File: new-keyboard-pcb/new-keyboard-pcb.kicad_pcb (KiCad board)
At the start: 2 copper layers, 392.5 x 125.2 mm, 226 parts, among them J1 Conn_ARM_JTAG_SWD_10, J2 Conn_01x05_Socket, J3 Conn_01x05_Pin, J4 Conn_01x05_Socket, J5 Conn_01x05_Pin, SW1 ESC, SW10 F9, SW100 SW_Push_Dual, SW11 F10, SW12 F11, SW13 F12, SW14 PWR, SW15 NUMLCK, SW16 DIV, SW17 MULT, SW18 SUB, SW19 /, SW2 F1, SW20 1, SW21 2, SW22 3, SW23 4, SW24 5, SW25 6, SW26 7, SW27 8, SW28 9, SW29 0, SW3 F2, SW30 -, SW31 =, SW32 DEL, SW33 #7, SW34 #8, SW35 #9, SW36 TAB, SW37 Q, SW38 W, SW39 E, SW4 F3, SW40 R, SW41 T, SW42 Y, SW43 U, SW44 I, SW45 O, SW46 P, SW47 ^, SW48 Ç, SW49 ENTER, SW5 F4, SW50 #4, SW51 #5, SW52 #6, SW53 ADD, SW54 CAPSLCK, SW55 A, SW56 S, SW57 D, SW58 F, SW59 G, SW6 F5, SW60 H, SW61 J, SW62 K, SW63 L, SW64 ;, SW65 È, SW66 À, SW67 ENTER, SW68 #1, SW69 #2, SW7 F6, SW70 #3, SW71 #ENTER, SW72 LSHFT, SW73 Ù, SW74 Z, SW75 X, SW76 C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

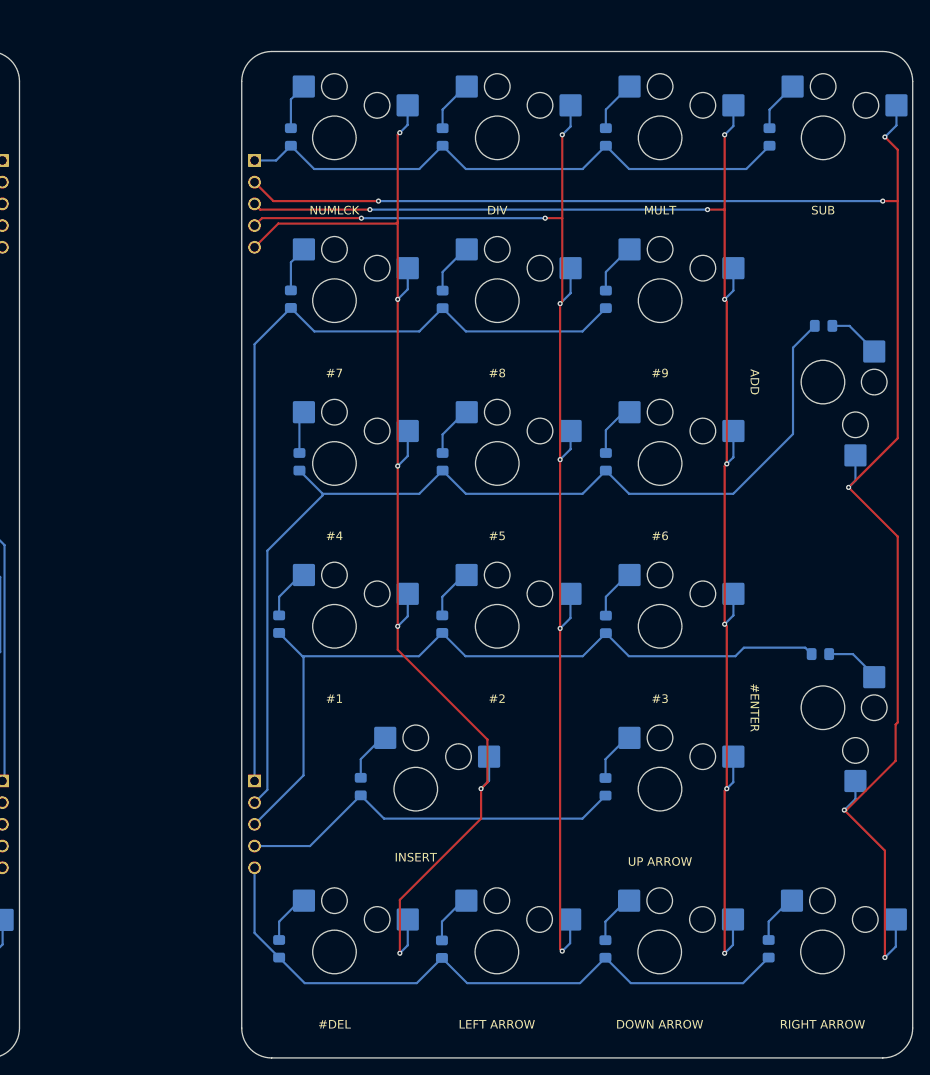
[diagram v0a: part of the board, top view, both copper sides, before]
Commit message: Correcting pogo connector connexions
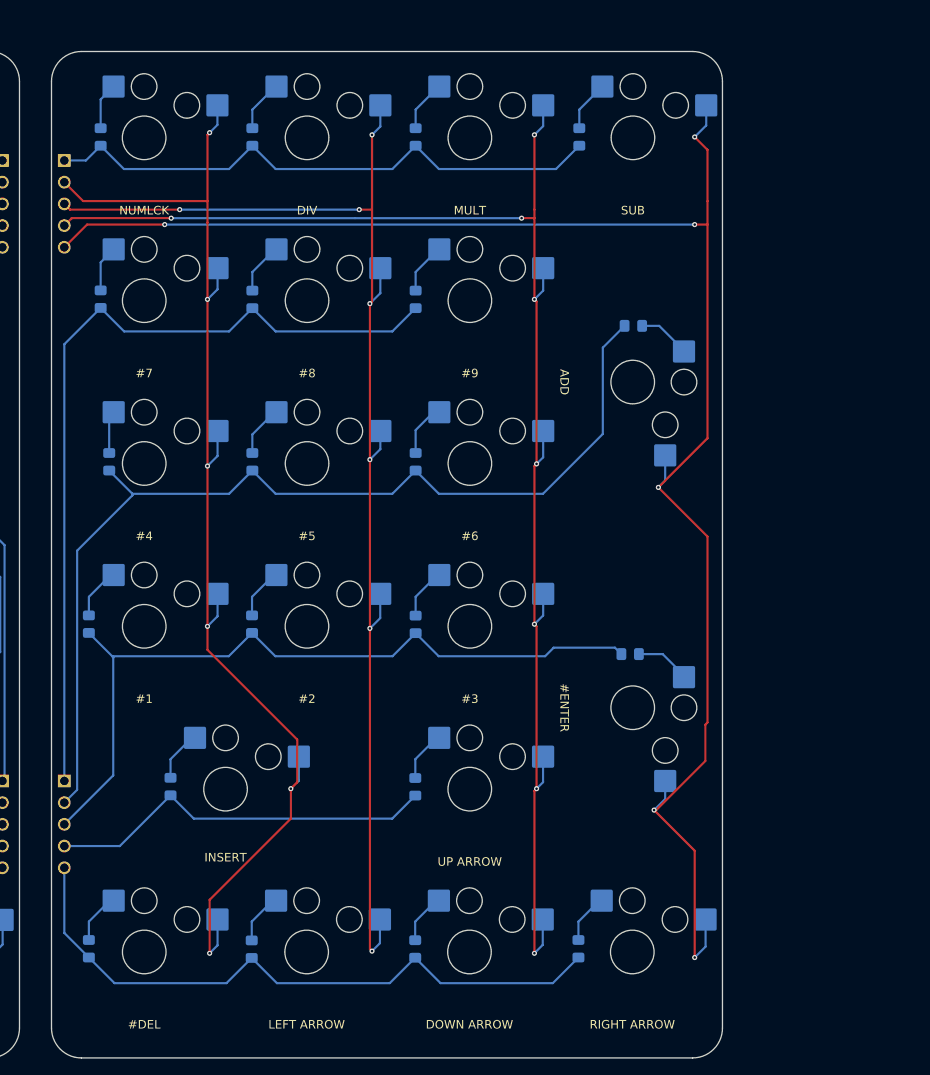
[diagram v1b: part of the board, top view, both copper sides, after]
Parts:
- J2, J4: footprint pogo_connector_5_pins:female -> pogo_connector_5_pins:connector
- J3, J5: footprint pogo_connector_5_pins:male -> pogo_connector_5_pins:connector
- moved D15 22.3 mm to (311.0, 42.0)
- moved D16 22.3 mm to (328.7, 42.0)
- moved D17 22.3 mm to (347.8, 42.0)
- moved D18 22.3 mm to (367.0, 42.0)
- moved D33 22.3 mm to (311.0, 61.0)
- moved D34 22.3 mm to (328.7, 61.0)
- moved D35 22.3 mm to (347.8, 61.0)
- moved D50 22.3 mm to (312.0, 80.0)
- moved D51 22.3 mm to (328.7, 80.0)
- moved D52 22.3 mm to (347.8, 80.0)
- moved D68 22.3 mm to (309.6, 99.0)
- moved D70 22.3 mm to (347.8, 99.0)
- moved D85 22.3 mm to (319.2, 118.0)
- moved D86 22.3 mm to (347.8, 118.0)
- moved D96 22.3 mm to (309.6, 137.0)
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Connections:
- J2 pad 1: ROW5B -> ROW1B
- J2 pad 2: ROW4B -> ROW2B
- J2 pad 4: ROW2B -> ROW4B
- J2 pad 5: ROW1B -> ROW5B
- J4 pad 1: COL17MAIN -> ROW0B
- J4 pad 2: COL16MAIN -> COL14MAIN
- J4 pad 4: COL14MAIN -> COL16MAIN
- J4 pad 5: ROW0B -> COL17MAIN
- J5 pad 2: COL17 -> COL14
- J5 pad 3: COL16 -> COL15
- J5 pad 4: COL15 -> COL16
- J5 pad 5: COL14 -> COL17
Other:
- board size 392.5 x 125.2 mm -> 370.2 x 125.2 mm

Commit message: added mounting holes
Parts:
- added REF**: MountingHole_2.2mm_M2, MountingHole:MountingHole_2.2mm_M2, F.Cu at (213.0, 137.5)
- added REF**: MountingHole_2.2mm_M2, MountingHole:MountingHole_2.2mm_M2, F.Cu at (19.5, 89.5)
- added REF**: MountingHole_2.2mm_M2, MountingHole:MountingHole_2.2mm_M2, F.Cu at (19.0, 48.0)
- added REF**: MountingHole_2.2mm_M2, MountingHole:MountingHole_2.2mm_M2, F.Cu at (118.5, 50.0)
- added REF**: MountingHole_2.2mm_M2, MountingHole:MountingHole_2.2mm_M2, F.Cu at (280.5, 91.5)
- added REF**: MountingHole_2.2mm_M2, MountingHole:MountingHole_2.2mm_M2, F.Cu at (365.0, 89.5)
- added REF**: MountingHole_2.2mm_M2, MountingHole:MountingHole_2.2mm_M2, F.Cu at (213.0, 87.5)
- added REF**: MountingHole_2.2mm_M2, MountingHole:MountingHole_2.2mm_M2, F.Cu at (378.5, 47.0)
- added REF**: MountingHole_2.2mm_M2, MountingHole:MountingHole_2.2mm_M2, F.Cu at (322.5, 45.0)
- added REF**: MountingHole_2.2mm_M2, MountingHole:MountingHole_2.2mm_M2, F.Cu at (27.5, 145.0)
- added REF**: MountingHole_2.2mm_M2, MountingHole:MountingHole_2.2mm_M2, F.Cu at (78.0, 126.5)
- added REF**: MountingHole_2.2mm_M2, MountingHole:MountingHole_2.2mm_M2, F.Cu at (321.0, 144.5)
- added REF**: MountingHole_2.2mm_M2, MountingHole:MountingHole_2.2mm_M2, F.Cu at (378.5, 141.5)
- added REF**: MountingHole_2.2mm_M2, MountingHole:MountingHole_2.2mm_M2, F.Cu at (113.5, 87.0)
- added REF**: MountingHole_2.2mm_M2, MountingHole:MountingHole_2.2mm_M2, F.Cu at (326.5, 89.5)
- added REF**: MountingHole_2.2mm_M2, MountingHole:MountingHole_2.2mm_M2, F.Cu at (275.5, 38.5)
- added REF**: MountingHole_2.2mm_M2, MountingHole:MountingHole_2.2mm_M2, F.Cu at (296.5, 145.0)
- added REF**: MountingHole_2.2mm_M2, MountingHole:MountingHole_2.2mm_M2, F.Cu at (213.5, 49.0)
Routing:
- net ROW0C: track 67.7 -> 69.6 mm
- net COL14: track 147.4 -> 148.1 mm

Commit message: modified mounting holes and re-outputed
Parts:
- moved REF** 23.2 mm to (313.5, 122.5)
- moved REF** 18.6 mm to (371.0, 124.5)
- moved REF** 16.0 mm to (280.5, 146.0)
- moved REF** 9.30 mm to (370.5, 82.0)
- moved REF** 8.51 mm to (373.0, 53.5)
- moved REF** 7.83 mm to (326.0, 52.0)
- moved REF** 6.96 mm to (120.0, 89.5)
- moved REF** 2.30 mm to (214.5, 89.2)
- moved REF** 2.02 mm to (27.8, 147.0)
- moved REF** 1.77 mm to (214.8, 50.2)
- moved REF** 1.58 mm to (280.0, 90.0)
- moved REF** 1.25 mm to (119.5, 50.8)
- moved REF** 1.25 mm to (77.2, 127.5)
- moved REF** 1.00 mm to (325.5, 89.5)
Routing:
- net COL17: track 199.7 -> 206.7 mm
- net ROW4C: track 45.8 -> 48.7 mm
- net COL16: track 176.0 -> 178.9 mm
- net COL15: track 153.0 -> 155.5 mm
- net ROW0C: track 69.6 -> 67.7 mm
- net COL14MAIN: track 293.8 -> 292.1 mm
- net COL15MAIN: track 293.1 -> 291.6 mm
- net COL16MAIN: track 293.0 -> 291.7 mm
- net COL17MAIN: track 294.1 -> 293.0 mm
- net COL14: track 148.1 -> 149.1 mm
